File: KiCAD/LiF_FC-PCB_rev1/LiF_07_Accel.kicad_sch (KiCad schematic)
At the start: 4 parts

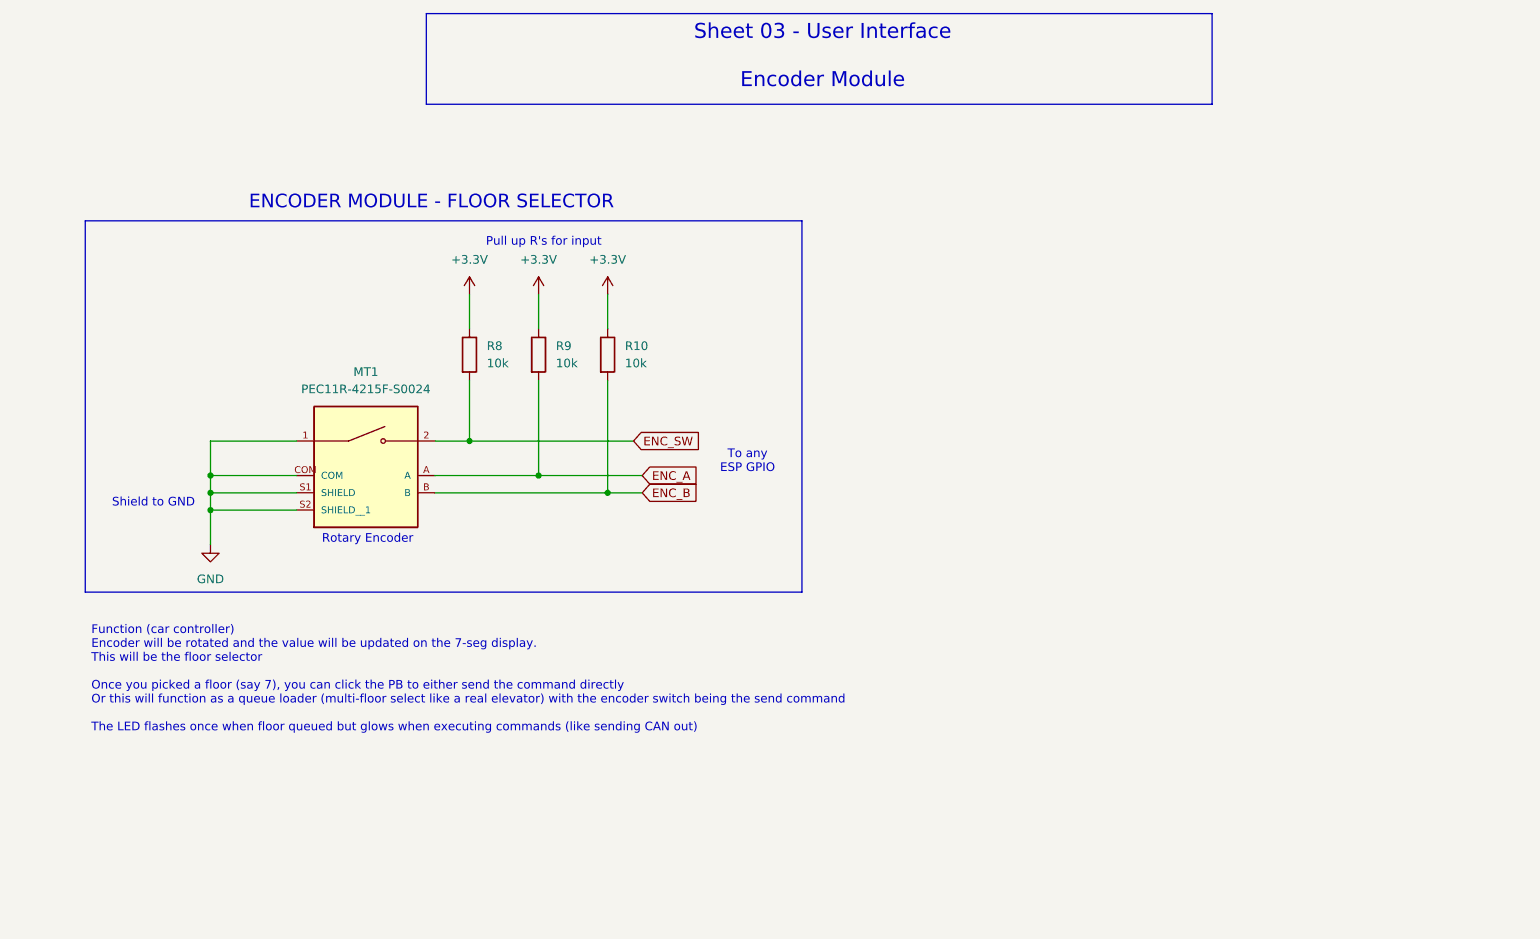
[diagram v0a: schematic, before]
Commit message: fixed my schematics syncing (I think), and added accelorometer schematic. Pushing since I need to switch main.
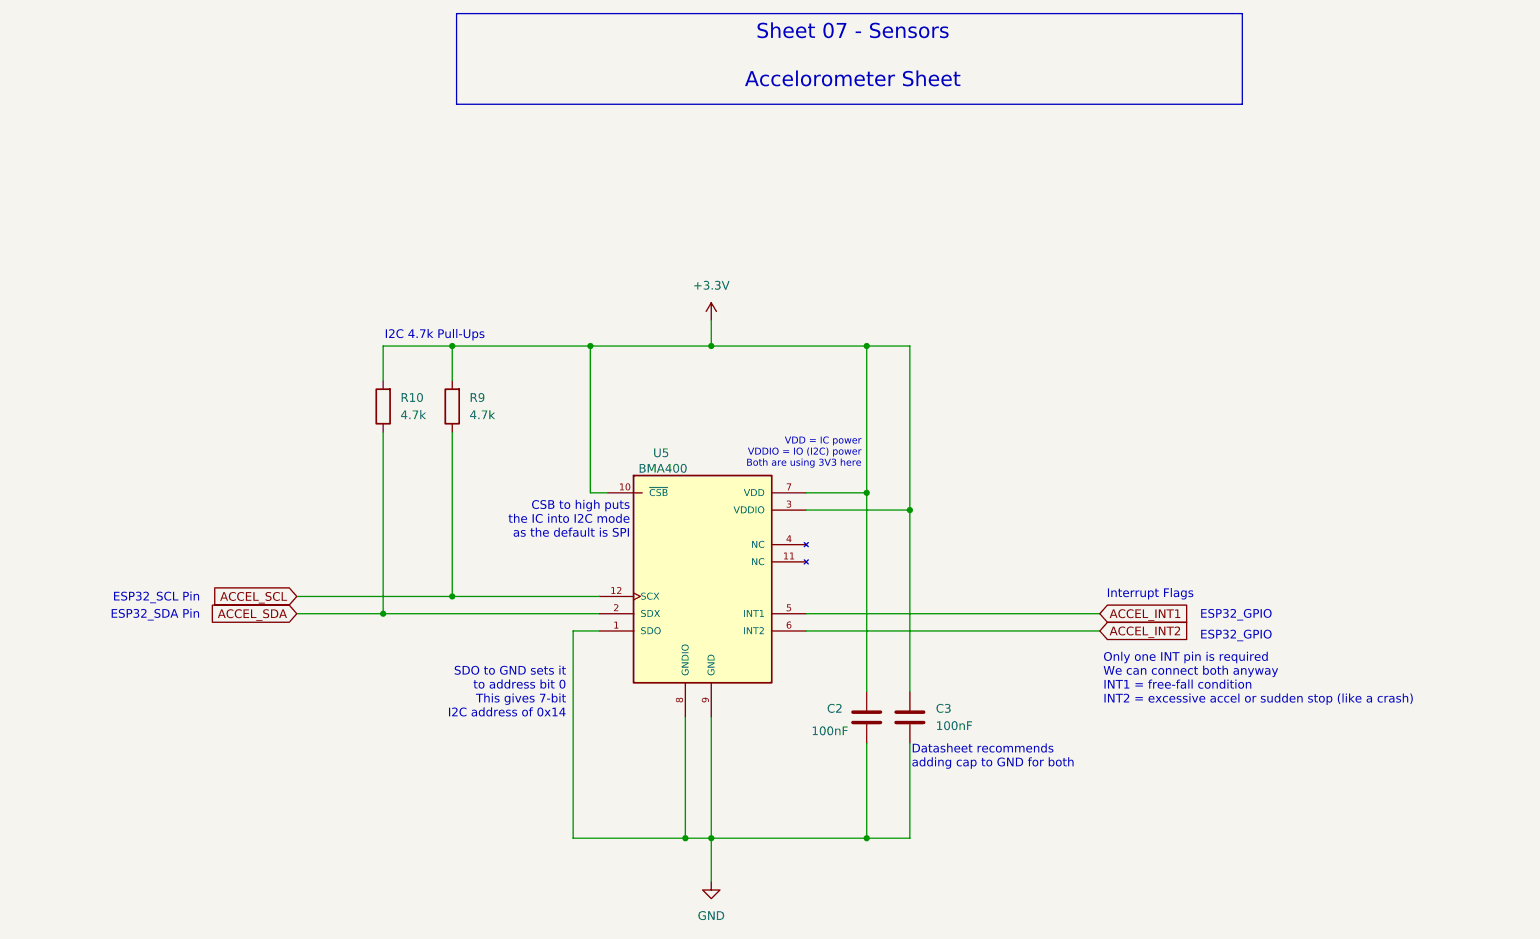
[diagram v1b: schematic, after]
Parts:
- removed MT1: PEC11R-4215F-S0024, PEC11R_4215F_S0024:XDCR_PEC11R-4215F-S0024, symbol PEC11R-4215F-S0024:PEC11R-4215F-S0024
- removed R8: 10k, Resistor_SMD:R_0805_2012Metric, symbol Device:R
- added C2, C3: 100nF, Capacitor_SMD:C_0805_2012Metric, symbol Device:C
- added U5: BMA400, Package_LGA:LGA-12_2x2mm_P0.5mm, symbol LiF_PCB_Symbols:BMA400
- R10, R9: value 10k -> 4.7k
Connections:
- net ENC_A is gone; now on net +3.3V: R9.2
- net ENC_B is gone; now on net +3.3V: R10.2
- net +3.3V: now also C2.1, C3.1, U5.10 (~{CSB}), U5.3 (VDDIO), U5.7 (VDD); no longer R10.1, R9.1
- net GND: now also C2.2, C3.2, U5.1 (SDO), U5.8 (GNDIO), U5.9 (GND)
- new net ACCEL_INT1: U5.5 (INT1)
- new net ACCEL_INT2: U5.6 (INT2)
- new net ACCEL_SCL: R9.1, U5.12 (SCX)
- new net ACCEL_SDA: R10.1, U5.2 (SDX)
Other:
- note added: "CSB to high puts the IC into I2C mode as the default is SPI"
- note added: "Datasheet recommends adding cap to GND for both"
- note added: "ESP32_GPIO"
- note added: "ESP32_SCL Pin"
- note added: "ESP32_SDA Pin"
- note added: "I2C 4.7k Pull-Ups"
- note added: "Interrupt Flags"
- note added: "Only one INT pin is required We can connect both anyway INT1 = free-fall condition INT2 = excessive accel or sudden stop (like a crash)"
- note added: "SDO to GND sets it to address bit 0 This gives 7-bit I2C address of 0x14"
- note added: "Sheet 07 - Sensors Accelorometer Sheet"
- note added: "VDD = IC power VDDIO = IO (I2C) power Both are using 3V3 here"
- note removed: "ENCODER MODULE - FLOOR SELECTOR"
- note removed: "Function (car controller) Encoder will be rotated and the value will be updated on the 7-seg display. This will be the floor selector Once you picked a floor (say 7), you can click the PB to either send the command directly Or this will function as a queue loader (multi-floor select like a real elevator) with the encoder switch being the send command The LED flashes once when floor queued but glo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"
- note removed: "Pull up R's for input"
- note removed: "Rotary Encoder"
- note removed: "Sheet 03 - User Interface Encoder Module"
- note removed: "Shield to GND"
- note removed: "To any ESP GPIO"

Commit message: updated schematics and pushing so MR can pull and begin merge.
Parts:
- renumbered C2 to C07_01, C3 to C07_02, R10 to R07_01, R9 to R07_02
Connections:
- net ACCEL_INT2 is gone; now on net ESP_ACCEL_INT1: U5.6 (INT2)
- net ACCEL_INT1 renamed ESP_ACCEL_INT1
- net ACCEL_SCL renamed ESP_ACCEL_SCL
- net ACCEL_SDA renamed ESP_ACCEL_SDA
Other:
- moved on the sheet: R07_01
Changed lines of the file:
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@@
 		)
 	)
-	(text "SDO to GND sets it\nto address bit 0\nThis gives 7-bit\nI2C address of 0x14"
+	(text "SDO to GND sets it\nto address bit 0\n\nThis gives 7-bit\nI2C address of 0x14"
 		(exclude_from_sim no)
 		(at 112.014 114.554 0)
@@
 	(text "ESP32_SDA Pin"
 		(exclude_from_sim no)
-		(at 58.166 103.124 0)
+		(at 47.498 103.124 0)
 		(effects
 			(font
@@
 	(text "ESP32_SCL Pin"
 		(exclude_from_sim no)
-		(at 58.166 100.584 0)
+		(at 47.498 100.584 0)
 		(effects
 			(font
@@
 	(text "ESP32_GPIO"
 		(exclude_from_sim no)
-		(at 205.232 106.172 0)
+		(at 209.042 105.918 0)
 		(effects
 			(font
@@
 	(text "ESP32_GPIO"
 		(exclude_from_sim no)
-		(at 205.232 103.124 0)
+		(at 209.042 102.87 0)
 		(effects
 			(font
@@
 	)
 	(junction
+		(at 83.82 102.87)
+		(diameter 0)
+		(color 0 0 0 0)
+	)
+	(junction
 		(at 115.57 63.5)
 		(diameter 0)
@@
 		(color 0 0 0 0)
 	)
-	(junction
-		(at 85.09 102.87)
-		(diameter 0)
-		(color 0 0 0 0)
-	)
 	(wire
 		(pts
@@
 	(wire
 		(pts
-			(xy 85.09 63.5) (xy 95.25 63.5)
+			(xy 83.82 63.5) (xy 95.25 63.5)
 		)
 		(stroke
@@
 	(wire
 		(pts
-			(xy 85.09 102.87) (xy 116.84 102.87)
-		)
-		(stroke
-			(width 0)
-			(type default)
-		)
-	)
-	(wire
-		(pts
 			(xy 113.03 105.41) (xy 116.84 105.41)
 		)
@@
 	(wire
 		(pts
-			(xy 85.09 76.2) (xy 85.09 102.87)
-		)
-		(stroke
-			(width 0)
-			(type default)
-		)
-	)
-	(wire
-		(pts
-			(xy 85.09 68.58) (xy 85.09 63.5)
+			(xy 83.82 102.87) (xy 116.84 102.87)
+		)
+		(stroke
+			(width 0)
+			(type default)
+		)
+	)
+	(wire
+		(pts
+			(xy 83.82 76.2) (xy 83.82 102.87)
+		)
+		(stroke
+			(width 0)
+			(type default)
+		)
+	)
+	(wire
+		(pts
+			(xy 83.82 68.58) (xy 83.82 63.5)
 		)
 		(stroke
@@
 	(wire
 		(pts
-			(xy 72.39 102.87) (xy 85.09 102.87)
+			(xy 72.39 102.87) (xy 83.82 102.87)
 		)
 		(stroke
@@
 		)
 	)
-	(global_label "ACCEL_INT2"
+	(hierarchical_label "ESP_ACCEL_INT1"
 		(shape input)
 		(at 190.5 105.41 0)
-		(fields_autoplaced yes)
 		(effects
 			(font
@@
 			(justify left)
 		)
-		(property "Intersheetrefs" "${INTERSHEET_REFS}"
-			(at 204.3709 105.41 0)
-			(effects
-				(font
-					(size 1.27 1.27)
-				)
-				(justify left)
-				(hide yes)
-			)
-		)
-	)
-	(global_label "ACCEL_INT1"
+	)
+	(hierarchical_label "ESP_ACCEL_INT1"
 		(shape input)
 		(at 190.5 102.87 0)
-		(fields_autoplaced yes)
 		(effects
 			(font
@@
 			(justify left)
 		)
-		(property "Intersheetrefs" "${INTERSHEET_REFS}"
-			(at 204.3709 102.87 0)
-			(effects
-				(font
-					(size 1.27 1.27)
-				)
-				(justify left)
-				(hide yes)
-			)
-		)
-	)
-	(global_label "ACCEL_SDA"
+	)
+	(hierarchical_label "ESP_ACCEL_SCL"
+		(shape input)
+		(at 72.39 100.33 180)
+		(effects
+			(font
+				(size 1.27 1.27)
+			)
+			(justify right)
+		)
+	)
+	(hierarchical_label "ESP_ACCEL_SDA"
 		(shape input)
 		(at 72.39 102.87 180)
-		(fields_autoplaced yes)
 		(effects
 			(font
@@
 			)
 			(justify right)
-		)
-		(property "Intersheetrefs" "${INTERSHEET_REFS}"
-			(at 59.0634 102.87 0)
-			(effects
-				(font
-					(size 1.27 1.27)
-				)
-				(justify right)
-				(hide yes)
-			)
-		)
-	)
-	(global_label "ACCEL_SCL"
-		(shape input)
-		(at 72.39 100.33 180)
-		(fields_autoplaced yes)
-		(effects
-			(font
-				(size 1.27 1.27)
-			)
-			(justify right)
-		)
-		(property "Intersheetrefs" "${INTERSHEET_REFS}"
-			(at 59.1239 100.33 0)
-			(effects
-				(font
-					(size 1.27 1.27)
-				)
-				(justify right)
-				(hide yes)
-			)
 		)
 	)
@@
 	(symbol
 		(lib_id "Device:R")
-		(at 85.09 72.39 180)
+		(at 83.82 72.39 180)
 		(unit 1)
 		(exclude_from_sim no)
@@
 		(dnp no)
 		(fields_autoplaced yes)
-		(property "Reference" "R10"
-			(at 87.63 71.1199 0)
+		(property "Reference" "R07_01"
+			(at 86.36 71.1199 0)
 			(effects
 				(font
@@
 		)
 		(property "Value" "4.7k"
-			(at 87.63 73.6599 0)
+			(at 86.36 73.6599 0)
 			(effects
 				(font
@@
 		)
 		(property "Footprint" "Resistor_SMD:R_0805_2012Metric"
-			(at 86.868 72.39 90)
+			(at 85.598 72.39 90)
 			(effects
 				(font
@@
 		)
 		(property "Datasheet" "~"
-			(at 85.09 72.39 0)
+			(at 83.82 72.39 0)
 			(effects
 				(font
@@
 		)
 		(property "Description" "Resistor"
-			(at 85.09 72.39 0)
+			(at 83.82 72.39 0)
 			(effects
 				(font
@@
 			(project "LiF_CustomPCB"
 				(path "/e8d53809-63ab-4a8d-88b7-d7504d15b103/bf38ce5a-6e0a-4fe9-8f4d-2cf211212732"
-					(reference "R10")
+					(reference "R07_01")
 					(unit 1)
 				)
@@
 		(dnp no)
 		(fields_autoplaced yes)
-		(property "Reference" "R9"
+		(property "Reference" "R07_02"
 			(at 97.79 71.1199 0)
 			(effects
@@
 			(project "LiF_CustomPCB"
 				(path "/e8d53809-63ab-4a8d-88b7-d7504d15b103/bf38ce5a-6e0a-4fe9-8f4d-2cf211212732"
-					(reference "R9")
+					(reference "R07_02")
 					(unit 1)
 				)
@@
 		(on_board yes)
 		(dnp no)
-		(property "Reference" "C2"
-			(at 150.368 116.84 0)
+		(property "Reference" "C07_01"
+			(at 146.558 117.348 0)
 			(effects
 				(font
@@
 			(project "LiF_CustomPCB"
 				(path "/e8d53809-63ab-4a8d-88b7-d7504d15b103/bf38ce5a-6e0a-4fe9-8f4d-2cf211212732"
-					(reference "C2")
+					(reference "C07_01")
 					(unit 1)
 				)
@@
 		(on_board yes)
 		(dnp no)
-		(fields_autoplaced yes)
-		(property "Reference" "C3"
-			(at 166.37 116.8399 0)
+		(property "Reference" "C07_02"
+			(at 166.37 117.094 0)
 			(effects
 				(font
@@
 			(project "LiF_CustomPCB"
 				(path "/e8d53809-63ab-4a8d-88b7-d7504d15b103/bf38ce5a-6e0a-4fe9-8f4d-2cf211212732"
-					(reference "C3")
+					(reference "C07_02")
 					(unit 1)
 				)
